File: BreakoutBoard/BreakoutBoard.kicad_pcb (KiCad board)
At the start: 0 parts

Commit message: Positions components on the PCB to match breadboard dimensions
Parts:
- added H1: ~, MountingHole:MountingHole_2.2mm_M2_Pad_Via, F.Cu at (130.8, 114.3)
- added H2: ~, MountingHole:MountingHole_2.2mm_M2_Pad_Via, F.Cu at (130.8, 83.8)
- added J1: addon_conn, GameOver:TXGA_FFC05036-24SBD113W5M_1x24_P0.50mm_Horizontal, F.Cu at (131.8, 100.3)
- added J2: Power_top, Connector_PinHeader_2.54mm:PinHeader_2x02_P2.54mm_Vertical, B.Cu at (129.5, 76.2)
- added J3: Power_bottom, Connector_PinHeader_2.54mm:PinHeader_2x02_P2.54mm_Vertical, B.Cu at (129.5, 124.5)
- added J4: Conn_01x09, Connector_PinHeader_2.54mm:PinHeader_1x09_P2.54mm_Vertical, B.Cu at (144.8, 96.5)
- added J5: Conn_01x10, Connector_PinHeader_2.54mm:PinHeader_1x10_P2.54mm_Vertical, B.Cu at (167.6, 104.1)
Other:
- copper layers 0 -> 2

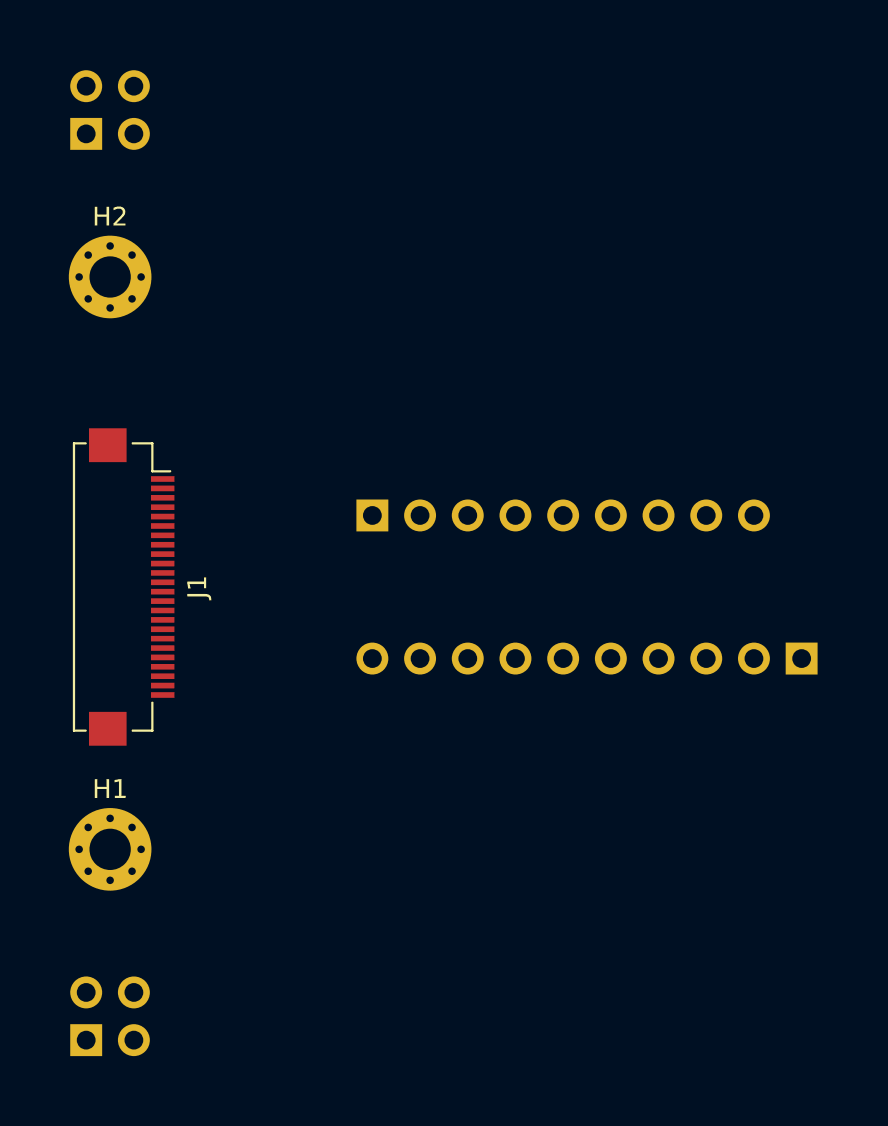
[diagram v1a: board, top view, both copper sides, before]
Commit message: Creates edge cuts for breakout board
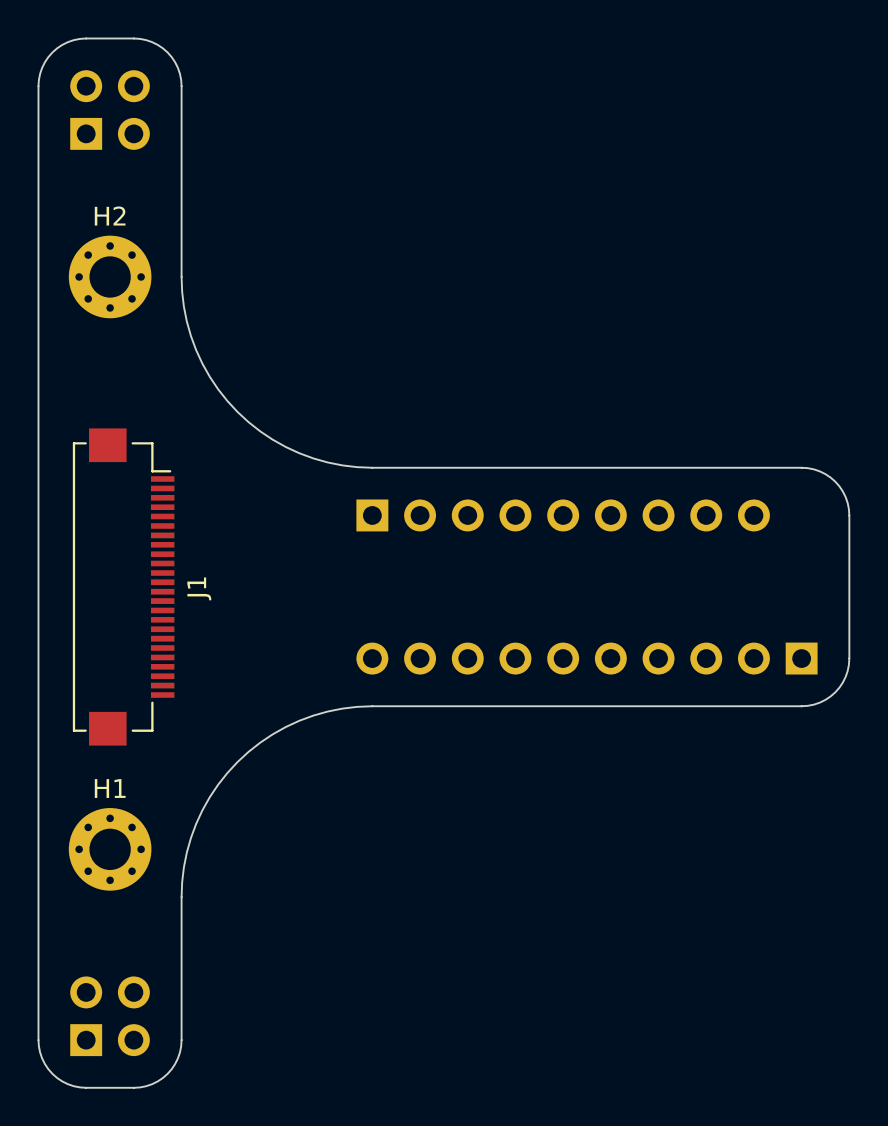
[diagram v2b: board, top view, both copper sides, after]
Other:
- board outline added: 43.2 x 55.9 mm
- board text added: "Power_top"

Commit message: Adds copper pours for GND and 3v3 on breakout board
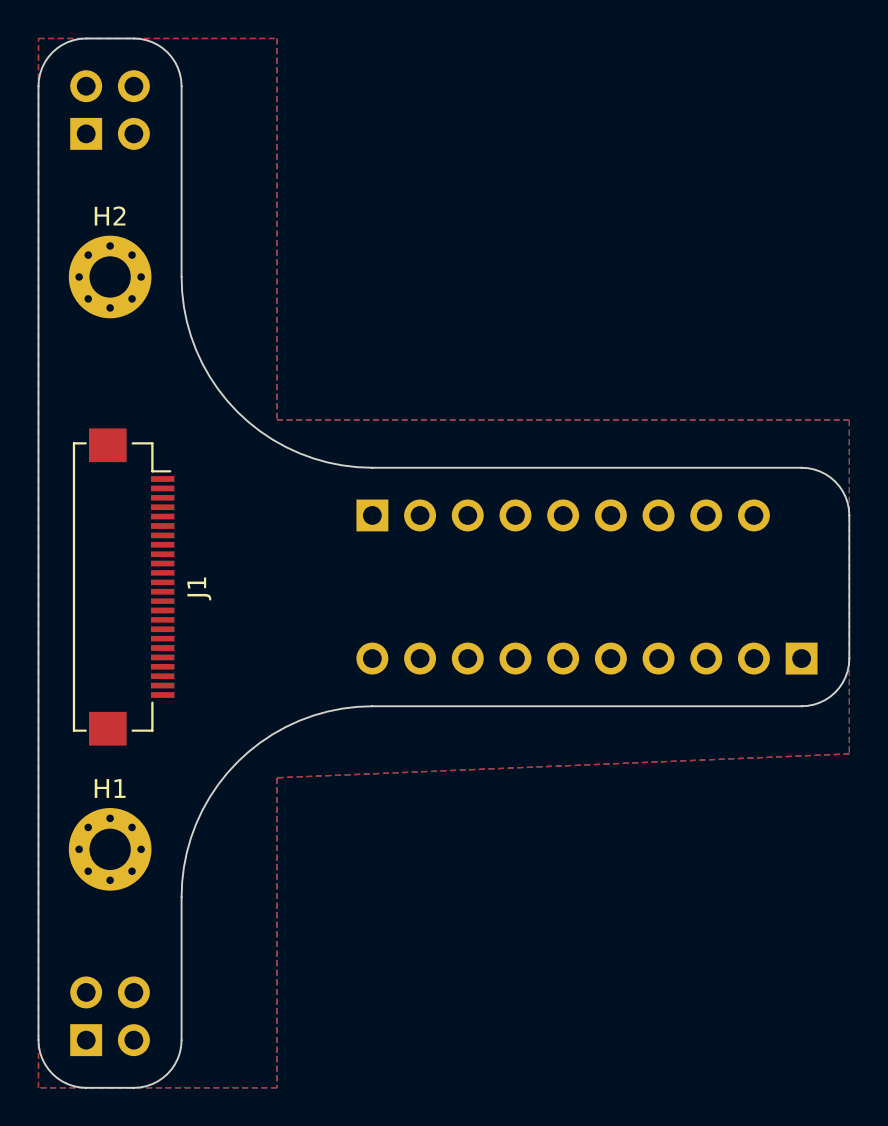
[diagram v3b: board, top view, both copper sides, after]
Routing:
- added copper zone on F.Cu, net +3V3
- added copper zone on B.Cu, net GND
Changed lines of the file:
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@@
     (effects (font (size 1 1) (thickness 0.15)) (justify mirror))
   )
+  (zone (net 2) (net_name "+3V3") (layer "F.Cu") (hatch edge 0.508)
+    (connect_pads (clearance 0.508))
+    (min_thickness 0.254) (filled_areas_thickness no)
+    (fill yes (thermal_gap 0.508) (thermal_bridge_width 0.508) (island_removal_mode 2) (island_area_min 9.999998))
+    (polygon
+      (pts
+        (xy 139.699827 91.438107)
+        (xy 170.179827 91.438107)
+        (xy 170.179827 109.218107)
+        (xy 139.699827 110.488107)
+        (xy 139.699827 126.998107)
+        (xy 126.999827 126.998107)
+        (xy 126.999827 71.118107)
+        (xy 139.699827 71.118107)
+      )
+    )
+  )
+  (zone (net 1) (net_name "GND") (layer "B.Cu") (hatch edge 0.508)
+    (connect_pads (clearance 0.508))
+    (min_thickness 0.254) (filled_areas_thickness no)
+    (fill yes (thermal_gap 0.508) (thermal_bridge_width 0.508) (island_removal_mode 2) (island_area_min 9.999999))
+    (polygon
+      (pts
+        (xy 139.7 91.44)
+        (xy 170.18 91.44)
+        (xy 170.18 109.22)
+        (xy 139.7 110.49)
+        (xy 139.7 127)
+        (xy 127 127)
+        (xy 127 71.12)
+        (xy 139.7 71.12)
+      )
+    )
+  )
 )

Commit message: Routes signals
I needed to route one single trace on the bottom layer :/
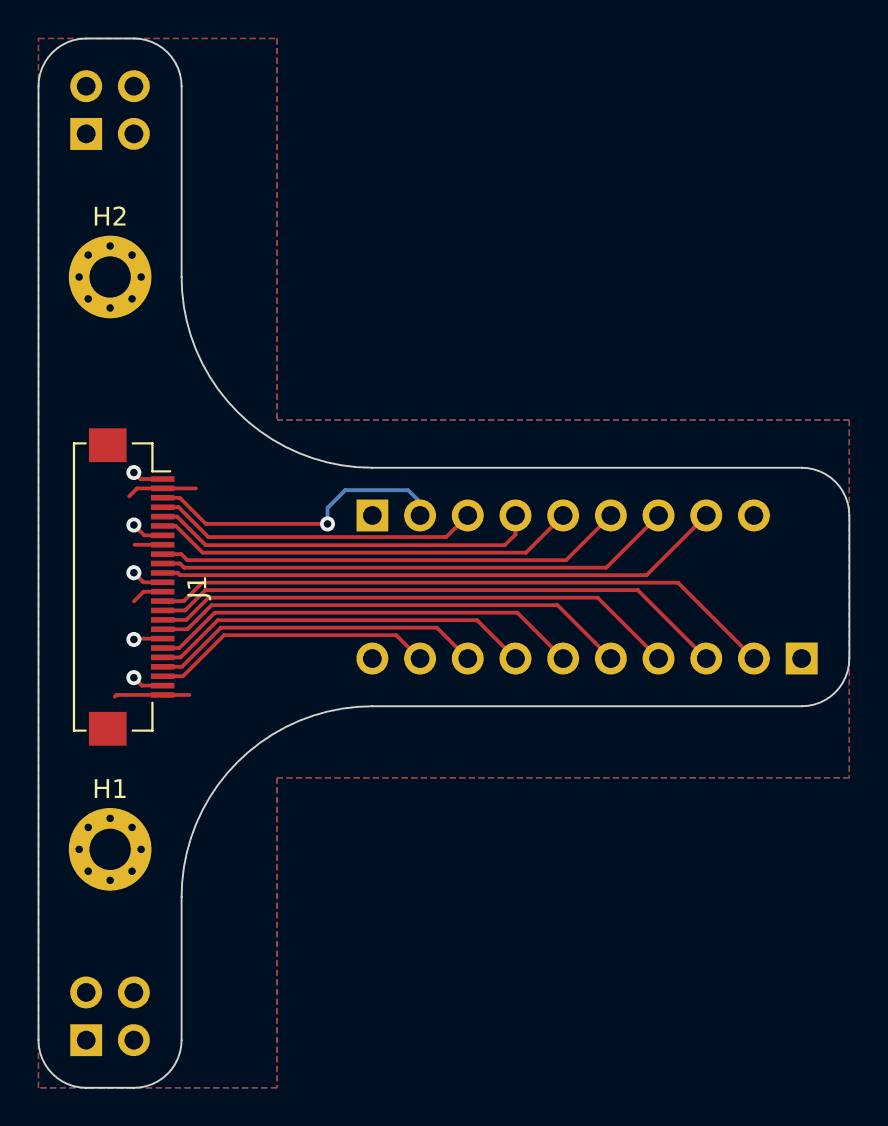
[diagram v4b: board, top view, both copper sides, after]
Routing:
- net Net-(J1-IO16): track 0.00 -> 33.6 mm
- net Net-(J1-IO4): track 0.00 -> 30.9 mm
- net Net-(J1-IO17): track 0.00 -> 30.3 mm
- net Net-(J1-IO2): track 0.00 -> 28.2 mm
- net Net-(J1-IO5): track 0.00 -> 27.6 mm
- net Net-(J1-IO15): track 0.00 -> 25.6 mm
- net Net-(J1-IO18): track 0.00 -> 25.0 mm
- net Net-(J1-IO34): track 0.00 -> 23.1 mm
- net Net-(J1-IO19): track 0.00 -> 22.7 mm
- net Net-(J1-IO21): track 0.00 -> 20.7 mm
- net Net-(J1-IO35): track 0.00 -> 20.5 mm
- net Net-(J1-IO32): track 0.00 -> 17.8 mm
- net Net-(J1-IO22): track 0.00 -> 17.4 mm
- net Net-(J1-IO23): track 0.00 -> 16.5 mm, vias 0 -> 1
- net Net-(J1-IO33): track 0.00 -> 15.1 mm
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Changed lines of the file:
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@@
 (kicad_pcb (version 20220331) (generator pcbnew)
   (general
-    (thickness 1.6)
+    (thickness 1.58)
   )
   (paper "A4")
@@
   )
   (setup
+    (stackup
+      (layer "F.Cu" (type "copper") (thickness 0.035))
+      (layer "dielectric 1" (type "core") (thickness 1.51) (material "FR4") (epsilon_r 4.5) (loss_tangent 0.02))
+      (layer "B.Cu" (type "copper") (thickness 0.035))
+      (copper_finish "None")
+      (dielectric_constraints no)
+    )
     (pad_to_mask_clearance 0)
     (pcbplotparams
@@
     (effects (font (size 1 1) (thickness 0.15)) (justify mirror))
   )
+  (segment (start 132.08 97.028) (end 132.632 97.58) (width 0.2) (layer "F.Cu") (net 1))
+  (segment (start 132.426 94.58) (end 133.615 94.58) (width 0.2) (layer "F.Cu") (net 1))
+  (segment (start 132.504 105.58) (end 133.615 105.58) (width 0.2) (layer "F.Cu") (net 1))
+  (segment (start 132.08 99.568) (end 132.592 100.08) (width 0.2) (layer "F.Cu") (net 1))
+  (segment (start 132.592 100.08) (end 133.615 100.08) (width 0.2) (layer "F.Cu") (net 1))
+  (segment (start 132.632 97.58) (end 133.615 97.58) (width 0.2) (layer "F.Cu") (net 1))
+  (segment (start 132.08 105.156) (end 132.504 105.58) (width 0.2) (layer "F.Cu") (net 1))
+  (segment (start 132.08 103.124) (end 132.124 103.08) (width 0.2) (layer "F.Cu") (net 1))
+  (segment (start 132.08 94.234) (end 132.426 94.58) (width 0.2) (layer "F.Cu") (net 1))
+  (segment (start 132.124 103.08) (end 133.615 103.08) (width 0.2) (layer "F.Cu") (net 1))
+  (via (at 132.08 105.156) (size 0.8) (drill 0.4) (layers "F.Cu" "B.Cu") (net 1))
+  (via (at 132.08 103.124) (size 0.8) (drill 0.4) (layers "F.Cu" "B.Cu") (net 1))
+  (via (at 132.08 99.568) (size 0.8) (drill 0.4) (layers "F.Cu" "B.Cu") (net 1))
+  (via (at 132.08 94.234) (size 0.8) (drill 0.4) (layers "F.Cu" "B.Cu") (net 1))
+  (via (at 132.08 97.028) (size 0.8) (drill 0.4) (layers "F.Cu" "B.Cu") (net 1))
+  (segment (start 133.615 106.08) (end 131.156 106.08) (width 0.2) (layer "F.Cu") (net 2))
+  (segment (start 133.615 106.08) (end 135.036 106.08) (width 0.2) (layer "F.Cu") (net 2))
+  (segment (start 133.615 95.08) (end 132.25 95.08) (width 0.2) (layer "F.Cu") (net 2))
+  (segment (start 133.615 95.08) (end 135.382 95.08) (width 0.2) (layer "F.Cu") (net 2))
+  (segment (start 131.156 106.08) (end 131.064 106.172) (width 0.2) (layer "F.Cu") (net 2))
+  (segment (start 132.596 100.58) (end 133.615 100.58) (width 0.2) (layer "F.Cu") (net 2))
+  (segment (start 132.116 98.08) (end 133.615 98.08) (width 0.2) (layer "F.Cu") (net 2))
+  (segment (start 132.25 95.08) (end 131.826 95.504) (width 0.2) (layer "F.Cu") (net 2))
+  (segment (start 132.084 101.092) (end 132.596 100.58) (width 0.2) (layer "F.Cu") (net 2))
+  (segment (start 142.3924 96.970011) (end 135.914417 96.970011) (width 0.2) (layer "F.Cu") (net 3))
+  (segment (start 134.524406 95.58) (end 133.615 95.58) (width 0.2) (layer "F.Cu") (net 3))
+  (segment (start 135.914417 96.970011) (end 134.524406 95.58) (width 0.2) (layer "F.Cu") (net 3))
+  (via (at 142.3924 96.970011) (size 0.8) (drill 0.4) (layers "F.Cu" "B.Cu") (net 3))
+  (segment (start 142.3924 96.970011) (end 142.3924 96.1136) (width 0.2) (layer "B.Cu") (net 3))
+  (segment (start 147.32 95.8088) (end 147.32 96.52) (width 0.2) (layer "B.Cu") (net 3))
+  (segment (start 143.3322 95.1738) (end 146.685 95.1738) (width 0.2) (layer "B.Cu") (net 3))
+  (segment (start 146.685 95.1738) (end 147.32 95.8088) (width 0.2) (layer "B.Cu") (net 3))
+  (segment (start 142.3924 96.1136) (end 143.3322 95.1738) (width 0.2) (layer "B.Cu") (net 3))
+  (segment (start 149.86 96.52) (end 148.710489 97.669511) (width 0.2) (layer "F.Cu") (net 4))
+  (segment (start 134.4594 96.08) (end 133.615 96.08) (width 0.2) (layer "F.Cu") (net 4))
+  (segment (start 136.048911 97.669511) (end 134.4594 96.08) (width 0.2) (layer "F.Cu") (net 4))
+  (segment (start 148.710489 97.669511) (end 136.048911 97.669511) (width 0.2) (layer "F.Cu") (net 4))
+  (segment (start 152.4 97.536) (end 151.834838 98.101162) (width 0.2) (layer "F.Cu") (net 5))
+  (segment (start 135.902568 98.101162) (end 134.381406 96.58) (width 0.2) (layer "F.Cu") (net 5))
+  (segment (start 134.381406 96.58) (end 133.615 96.58) (width 0.2) (layer "F.Cu") (net 5))
+  (segment (start 152.4 96.52) (end 152.4 97.536) (width 0.2) (layer "F.Cu") (net 5))
+  (segment (start 151.834838 98.101162) (end 135.902568 98.101162) (width 0.2) (layer "F.Cu") (net 5))
+  (segment (start 154.94 96.52) (end 152.959318 98.500682) (width 0.2) (layer "F.Cu") (net 6))
+  (segment (start 152.959318 98.500682) (end 135.737082 98.500682) (width 0.2) (layer "F.Cu") (net 6))
+  (segment (start 135.737082 98.500682) (end 134.3164 97.08) (width 0.2) (layer "F.Cu") (net 6))
+  (segment (start 134.3164 97.08) (end 133.615 97.08) (width 0.2) (layer "F.Cu") (net 6))
+  (segment (start 157.48 96.52) (end 155.099798 98.900202) (width 0.2) (layer "F.Cu") (net 7))
+  (segment (start 155.099798 98.900202) (end 134.923608 98.900202) (width 0.2) (layer "F.Cu") (net 7))
+  (segment (start 134.923608 98.900202) (end 134.603406 98.58) (width 0.2) (layer "F.Cu") (net 7))
+  (segment (start 134.603406 98.58) (end 133.615 98.58) (width 0.2) (layer "F.Cu") (net 7))
+  (segment (start 134.758122 99.299722) (end 157.240278 99.299722) (width 0.2) (layer "F.Cu") (net 8))
+  (segment (start 157.240278 99.299722) (end 160.02 96.52) (width 0.2) (layer "F.Cu") (net 8))
+  (segment (start 134.5384 99.08) (end 134.758122 99.299722) (width 0.2) (layer "F.Cu") (net 8))
+  (segment (start 133.615 99.08) (end 134.5384 99.08) (width 0.2) (layer "F.Cu") (net 8))
+  (segment (start 134.420269 99.58) (end 133.615 99.58) (width 0.2) (layer "F.Cu") (net 9))
+  (segment (start 159.380758 99.699242) (end 134.539511 99.699242) (width 0.2) (layer "F.Cu") (net 9))
+  (segment (start 162.56 96.52) (end 159.380758 99.699242) (width 0.2) (layer "F.Cu") (net 9))
+  (segment (start 134.539511 99.699242) (end 134.420269 99.58) (width 0.2) (layer "F.Cu") (net 9))
+  (segment (start 135.722196 100.098762) (end 134.740958 101.08) (width 0.2) (layer "F.Cu") (net 10))
+  (segment (start 134.740958 101.08) (end 133.615 101.08) (width 0.2) (layer "F.Cu") (net 10))
+  (segment (start 161.058762 100.098762) (end 135.722196 100.098762) (width 0.2) (layer "F.Cu") (net 10))
+  (segment (start 165.1 104.14) (end 161.058762 100.098762) (width 0.2) (layer "F.Cu") (net 10))
+  (segment (start 158.918281 100.498281) (end 135.887683 100.498281) (width 0.2) (layer "F.Cu") (net 11))
+  (segment (start 134.805964 101.58) (end 133.615 101.58) (width 0.2) (layer "F.Cu") (net 11))
+  (segment (start 162.56 104.14) (end 158.918281 100.498281) (width 0.2) (layer "F.Cu") (net 11))
+  (segment (start 135.887683 100.498281) (end 134.805964 101.58) (width 0.2) (layer "F.Cu") (net 11))
+  (segment (start 160.02 104.14) (end 156.777801 100.897801) (width 0.2) (layer "F.Cu") (net 12))
+  (segment (start 134.87097 102.08) (end 133.615 102.08) (width 0.2) (layer "F.Cu") (net 12))
+  (segment (start 156.777801 100.897801) (end 136.053169 100.897801) (width 0.2) (layer "F.Cu") (net 12))
+  (segment (start 136.053169 100.897801) (end 134.87097 102.08) (width 0.2) (layer "F.Cu") (net 12))
+  (segment (start 154.63732 101.29732) (end 136.218656 101.29732) (width 0.2) (layer "F.Cu") (net 13))
+  (segment (start 134.935976 102.58) (end 133.615 102.58) (width 0.2) (layer "F.Cu") (net 13))
+  (segment (start 157.48 104.14) (end 154.63732 101.29732) (width 0.2) (layer "F.Cu") (net 13))
+  (segment (start 136.218656 101.29732) (end 134.935976 102.58) (width 0.2) (layer "F.Cu") (net 13))
+  (segment (start 136.384142 101.69684) (end 152.49684 101.69684) (width 0.2) (layer "F.Cu") (net 14))
+  (segment (start 133.615 103.58) (end 134.500982 103.58) (width 0.2) (layer "F.Cu") (net 14))
+  (segment (start 152.49684 101.69684) (end 154.94 104.14) (width 0.2) (layer "F.Cu") (net 14))
+  (segment (start 134.500982 103.58) (end 136.384142 101.69684) (width 0.2) (layer "F.Cu") (net 14))
+  (segment (start 134.565988 104.08) (end 133.615 104.08) (width 0.2) (layer "F.Cu") (net 15))
+  (segment (start 150.35636 102.09636) (end 136.549628 102.09636) (width 0.2) (layer "F.Cu") (net 15))
+  (segment (start 152.4 104.14) (end 150.35636 102.09636) (width 0.2) (layer "F.Cu") (net 15))
+  (segment (start 136.549628 102.09636) (end 134.565988 104.08) (width 0.2) (layer "F.Cu") (net 15))
+  (segment (start 136.715114 102.49588) (end 148.21588 102.49588) (width 0.2) (layer "F.Cu") (net 16))
+  (segment (start 134.630994 104.58) (end 136.715114 102.49588) (width 0.2) (layer "F.Cu") (net 16))
+  (segment (start 133.615 104.58) (end 134.630994 104.58) (width 0.2) (layer "F.Cu") (net 16))
+  (segment (start 148.21588 102.49588) (end 149.86 104.14) (width 0.2) (layer "F.Cu") (net 16))
+  (segment (start 147.2946 104.14) (end 146.05 102.8954) (width 0.2) (layer "F.Cu") (net 17))
+  (segment (start 147.32 104.14) (end 147.2946 104.14) (width 0.2) (layer "F.Cu") (net 17))
+  (segment (start 146.05 102.8954) (end 136.8806 102.8954) (width 0.2) (layer "F.Cu") (net 17))
+  (segment (start 136.8806 102.8954) (end 134.696 105.08) (width 0.2) (layer "F.Cu") (net 17))
+  (segment (start 134.696 105.08) (end 133.615 105.08) (width 0.2) (layer "F.Cu") (net 17))
   (zone (net 2) (net_name "+3V3") (layer "F.Cu") (hatch edge 0.508)
     (connect_pads (clearance 0.508))
@@
         (xy 139.699827 91.438107)
         (xy 170.179827 91.438107)
-        (xy 170.179827 109.218107)
+        (xy 170.18 110.49)
         (xy 139.699827 110.488107)
         (xy 139.699827 126.998107)
@@
         (xy 139.7 91.44)
         (xy 170.18 91.44)
-        (xy 170.18 109.22)
+        (xy 170.18 110.49)
         (xy 139.7 110.49)
         (xy 139.7 127)
